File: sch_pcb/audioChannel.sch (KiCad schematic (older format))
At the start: 86 parts, among them J204 DE9F, Q201 BSS138, Q202 BSS138, Q203 BSS138, U103 MCP4351, U201 MCP6004T, U202 74LVC1G3157, U203 74LVC1G3157, U204 74LVC4066, U205 MCP6004T, U206 74LVC1G3157, U207 MCP6S26, U408 MCP23008

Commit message: Change 33pf to 100pf.  Change 2k and 2200 to 2k2.  Change I2C addresses for MCP23008.  Nudge link connectors
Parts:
- C203, C211, C213, C217, C219: value 33p -> 100p
- R212, R215, R219, R226: value 2k -> 2k2
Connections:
- net GND: no longer U408.4 (A1)
- net I2C_ADDR: now also U408.4 (A1); no longer U408.5 (A0)
- net at R227.1, U408.6 (~RESET): now also U408.5 (A0)
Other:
- moved on the sheet: R426, R427, U404A, U404B, U404C, U404D

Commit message: Add files via upload
Fix i2c addressing
Change footprint for LDR
Move connectors for temp/hum sensor and rtc so they won't hit the Pi
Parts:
- R216, R218: value 50k -> 51k
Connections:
- net at R227.1, U408.6 (~RESET): no longer U408.5 (A0)
- net I2C_ADDR renamed I2C_ADDR_1
- new net I2C_ADDR_0: U408.5 (A0)
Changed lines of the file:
@@
 AR Path="/596DD0D0/591BBEB4" Ref="R416"  Part="1"
 F 0 "R416" V 5630 4925 50  0000 C CNN
-F 1 "50k" V 5550 4925 50  0000 C CNN
+F 1 "51k" V 5550 4925 50  0000 C CNN
 F 2 "lib:smd0603" V 5480 4925 50  0001 C CNN
 F 3 "" H 5550 4925 50  0001 C CNN
@@
 AR Path="/596DD0D0/591BBF5A" Ref="R418"  Part="1"
 F 0 "R418" V 6030 5225 50  0000 C CNN
-F 1 "50k" V 5950 5225 50  0000 C CNN
+F 1 "51k" V 5950 5225 50  0000 C CNN
 F 2 "lib:smd0603" V 5880 5225 50  0001 C CNN
 F 3 "" H 5950 5225 50  0001 C CNN
@@
 	1375 1575 1700 1575
 Text HLabel 1450 1975 0    60   Input ~ 0
-I2C_ADDR
+I2C_ADDR_1
 Wire Wire Line
 	1575 2075 1575 2325
@@
 Wire Wire Line
 	1700 2075 1575 2075
-Connection ~ 1575 2075
 $Comp
 L MCP344XD U103
@@
 Connection ~ 8075 4925
 Wire Wire Line
-	1700 1875 1625 1875
-Wire Wire Line
-	1625 1875 1625 1325
-Connection ~ 1625 1325
-Wire Wire Line
 	1700 1975 1450 1975
+Text HLabel 1450 1875 0    60   Input ~ 0
+I2C_ADDR_0
+Wire Wire Line
+	1450 1875 1700 1875
 $EndSCHEMATC

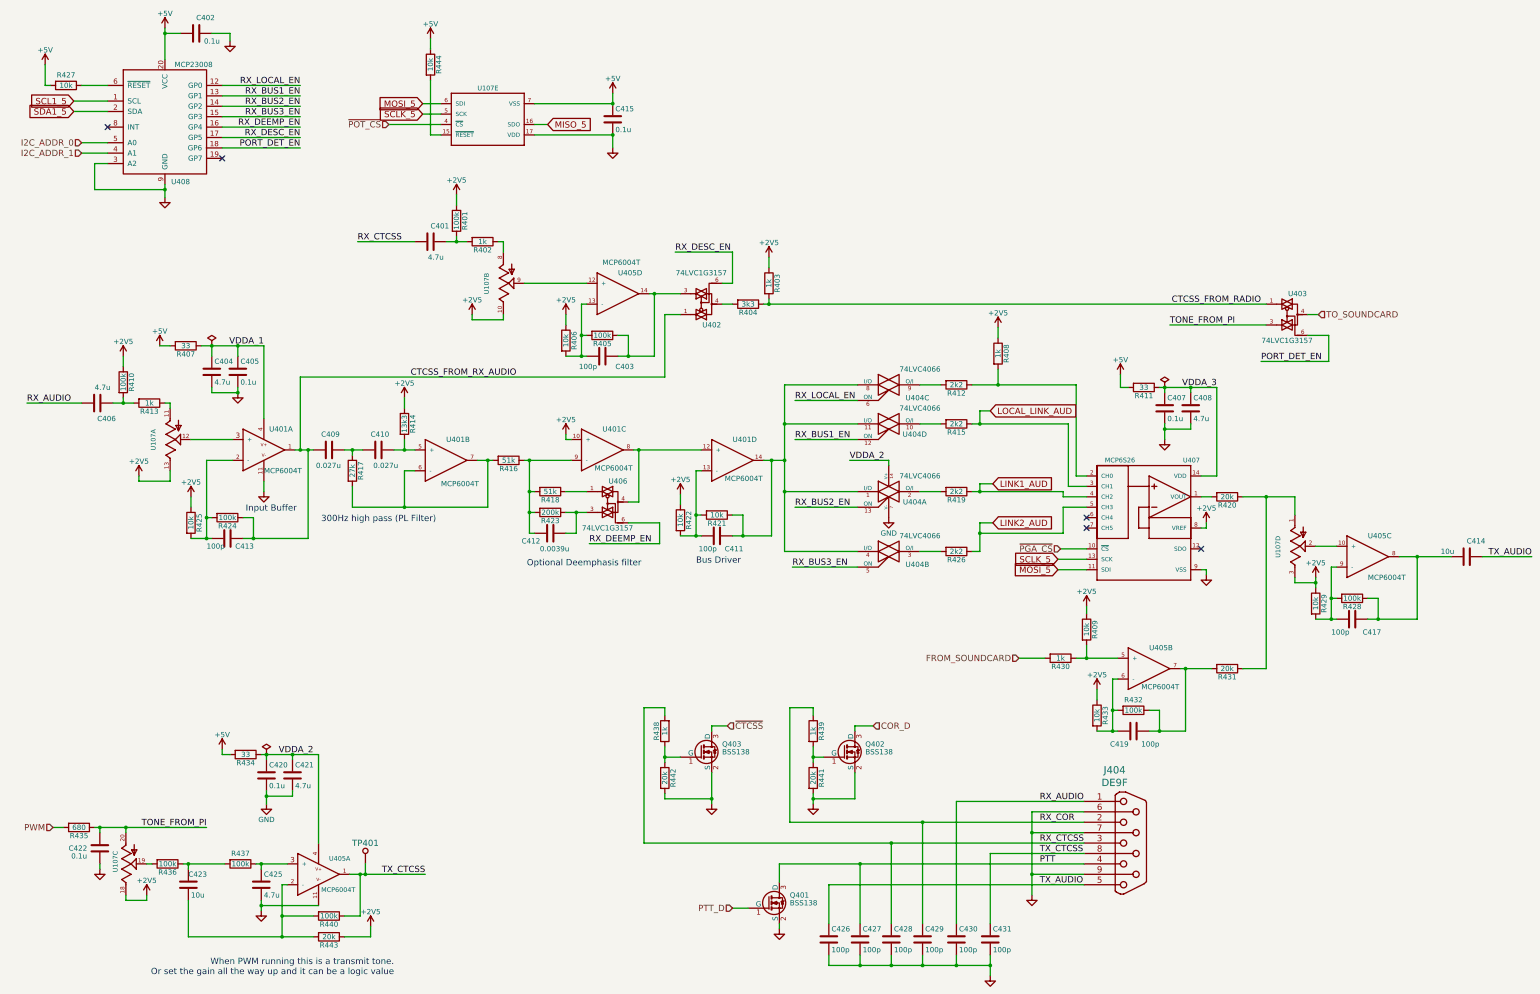
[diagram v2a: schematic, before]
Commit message: Add Digikey part # to all parts.  Fix unconnected nets
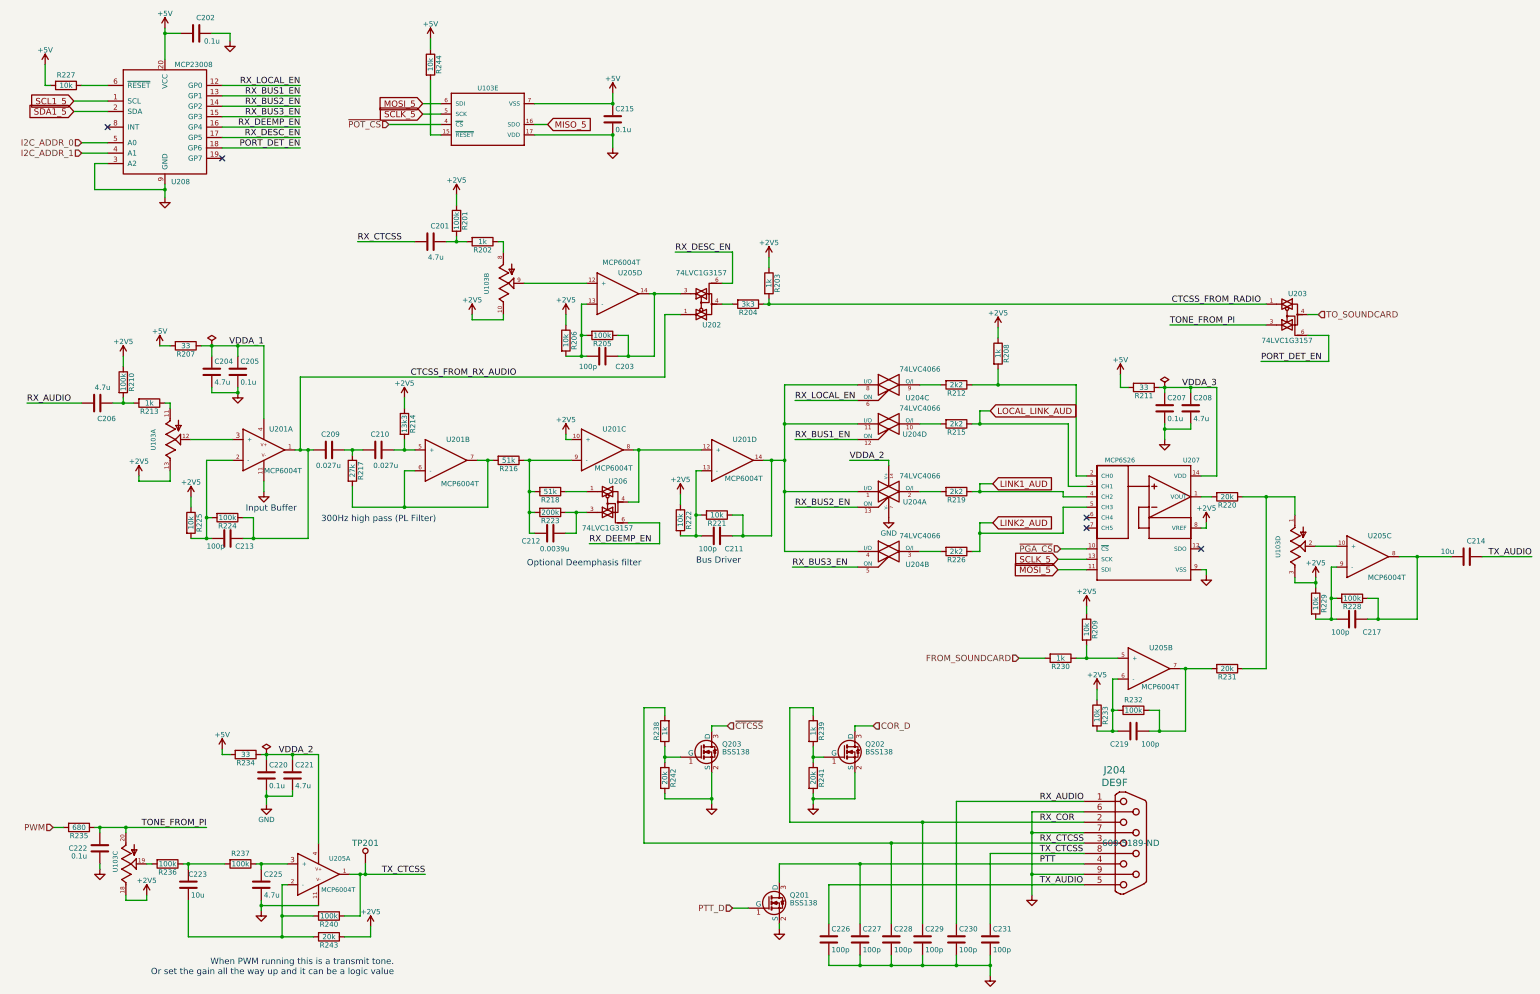
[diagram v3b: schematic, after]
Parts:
- C201, C204, C206, C208, C221, C225: Digikey PN (none) -> 1276-2087-1-ND
- C202, C205, C207, C220, C222, C415: Digikey PN (none) -> 399-1096-1-ND
- C203, C211, C213, C217, C219, C227, C228, C231, C426, C429, C430: Digikey PN (none) -> 399-1061-1-ND
- C209, C210: Digikey PN (none) -> 399-7891-1-ND
- C212: Digikey PN (none) -> 399-7913-1-ND
- C214, C223: Digikey PN (none) -> 478-5165-1-ND
- J204: Digikey PN (none) -> 609-5189-ND
- Q201, Q202, Q203: Digikey PN (none) -> 7-1142-1-ND
- R201, R205, R210, R224, R228, R232, R236, R237, R240: Digikey PN (none) -> 311-100KGRCT-ND
- R202, R203, R208, R213, R230, R238, R239: Digikey PN (none) -> 311-1.0KGRCT-ND
- R204: Digikey PN (none) -> 311-3.3KGRCT-ND
- R206, R209, R221, R222, R225, R227, R229, R233, R244: Digikey PN (none) -> 311-10KGRCT-ND
- R207, R211, R234: Digikey PN (none) -> 311-33GRCT-ND
- R212, R215, R219, R226: Digikey PN (none) -> 311-2.2KGRCT-ND
- R214: Digikey PN (none) -> 311-13.3KHRCT-ND
- R216, R218: Digikey PN (none) -> 311-51KGRCT-ND
- R217: Digikey PN (none) -> 311-27KGRCT-ND
- R220, R231, R241, R242, R243: Digikey PN (none) -> 311-20KGRCT-ND
- R223: Digikey PN (none) -> 311-200KGRCT-ND
- R235: Digikey PN (none) -> 311-680GRCT-ND
- U103: Digikey PN (none) -> MCP4351-103E/ST-ND
- U201, U205: Digikey PN (none) -> MCP6004-I/SL-ND
- U202, U203, U206: Digikey PN (none) -> 296-14908-1-ND
- U204: Digikey PN (none) -> 1727-6368-1-ND
- U207: Digikey PN (none) -> MCP6S26-I/SL-ND
- U408: Digikey PN (none) -> MCP23008-E/SS-ND

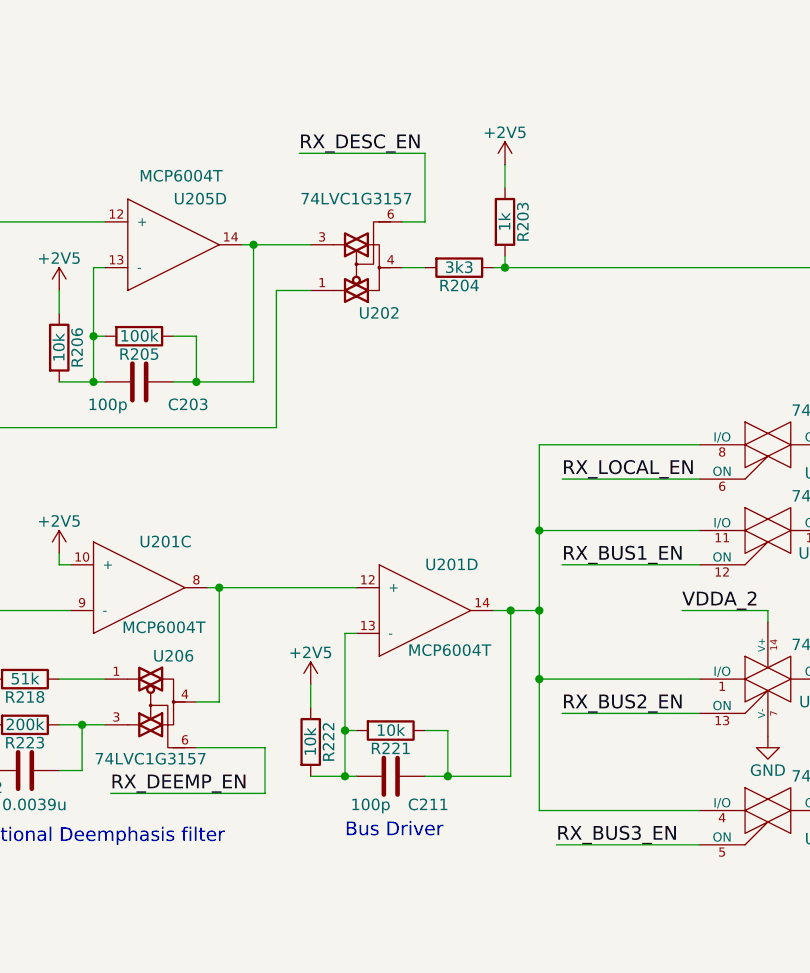
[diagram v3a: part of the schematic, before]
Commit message: Switch to 0402 parts and SeeedStudio footprints
Silk screen is still being updated.  BOM needs to be updated as well
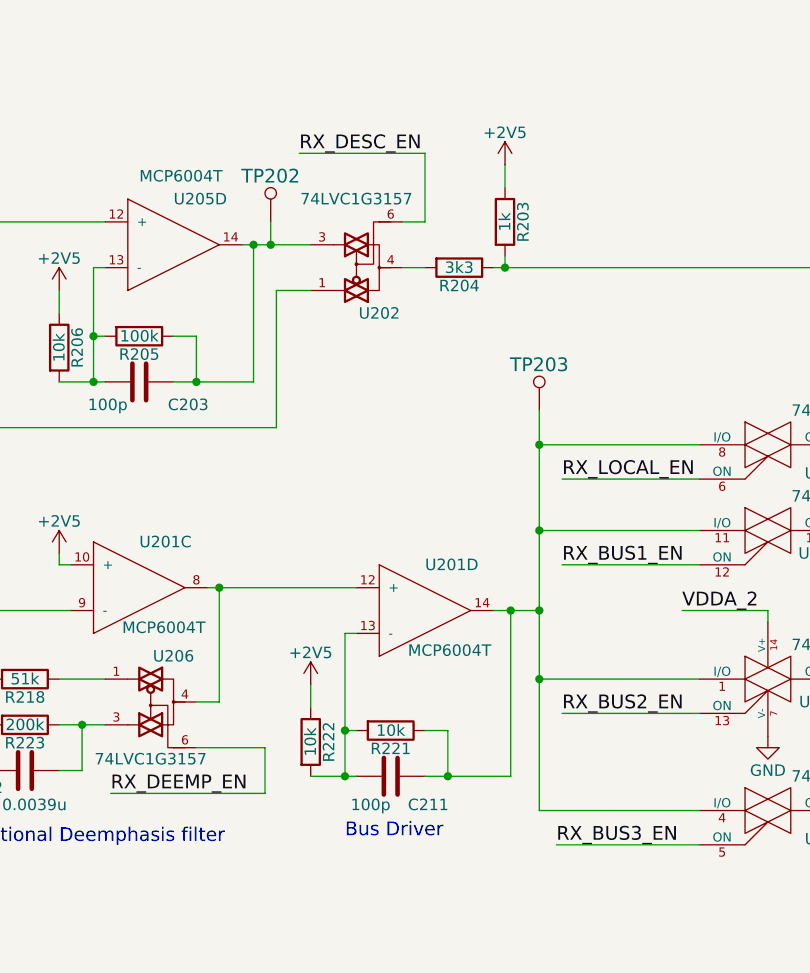
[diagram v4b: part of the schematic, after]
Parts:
- added TP203, TP402: TESTPOINT, lib:Wire_28AWG, symbol TESTPOINT
- C201, C202, C203, C204, C205, C206, C207, C208, C209, C210, C211, C212, C213, C217, C219, C220, C221, C222, C225, C227, C228, C231, C415, C426, C429, C430: footprint lib:smd0603 -> lib:OPL_C0402
- C214, C223: footprint lib:smd0805 -> lib:OPL_C0603
- Q201, Q202, Q203: footprint lib:SOT23 -> lib:OPL_SOT-23
- R201, R202, R203, R204, R205, R206, R207, R208, R209, R210, R211, R212, R213, R214, R215, R216, R217, R218, R219, R220, R221, R222, R223, R224, R225, R226, R227, R228, R229, R230, R231, R232, R233, R234, R235, R236, R237, R238, R239, R240, R241, R242, R243, R244: footprint lib:smd0603 -> lib:OPL_R0402
- U103, U408: footprint lib:SSOP-20 -> lib:OPL_TSSOP20-0.65-6.5X4.4MM
- U202, U203, U206: footprint lib:SOT23-6 -> lib:OPL_SOT-23-6
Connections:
- net at C203.1, R205.1, U202.3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: now also TP402.1
- net at C211.1, R221.1, U201.14 (OUT)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: now also TP203.1
